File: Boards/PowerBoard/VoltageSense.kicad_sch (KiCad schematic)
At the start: 40 parts

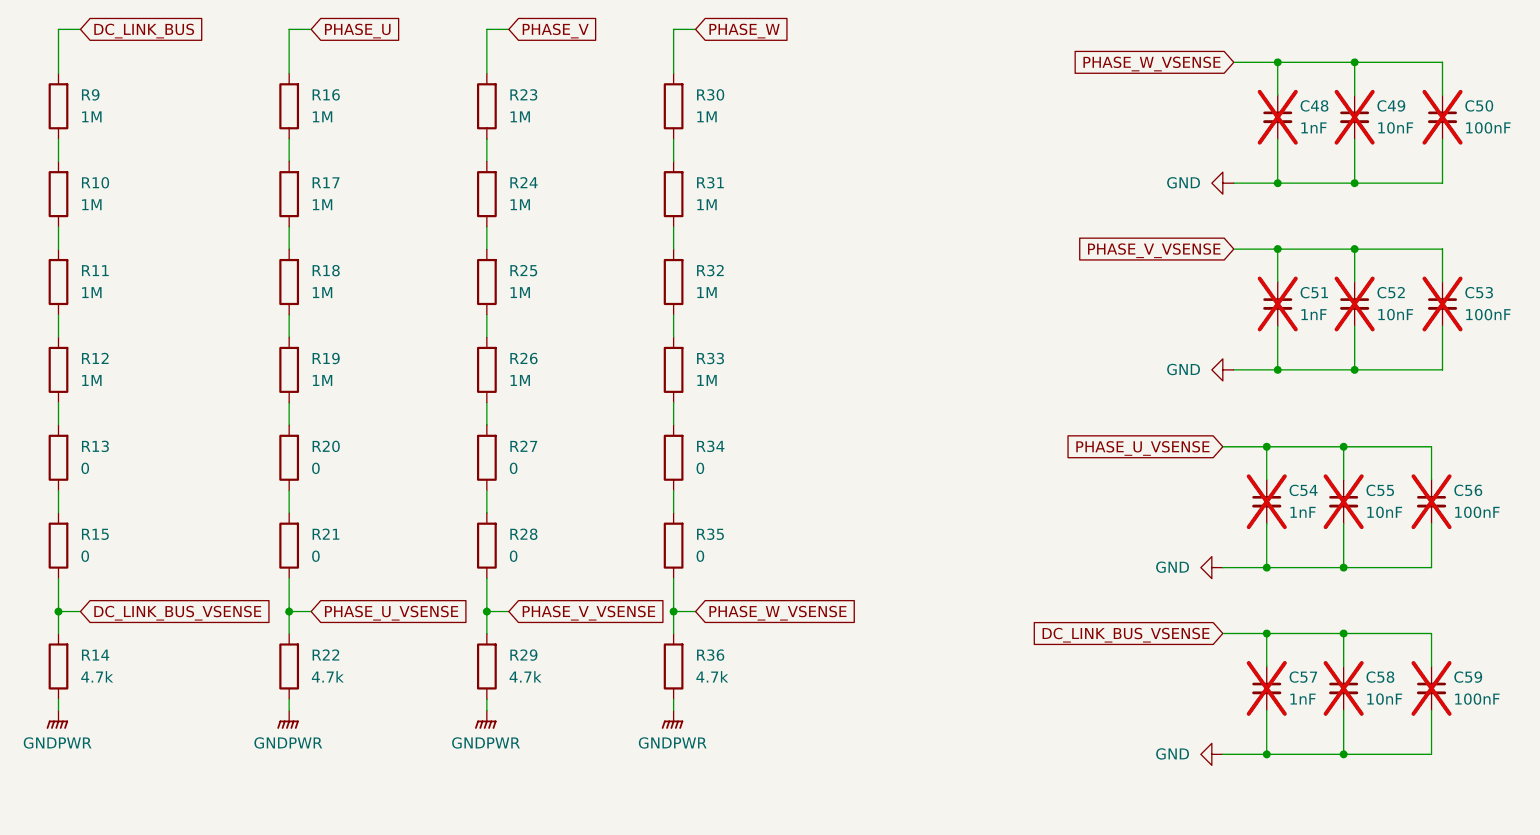
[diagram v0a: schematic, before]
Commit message: Add Zeners to Power Board
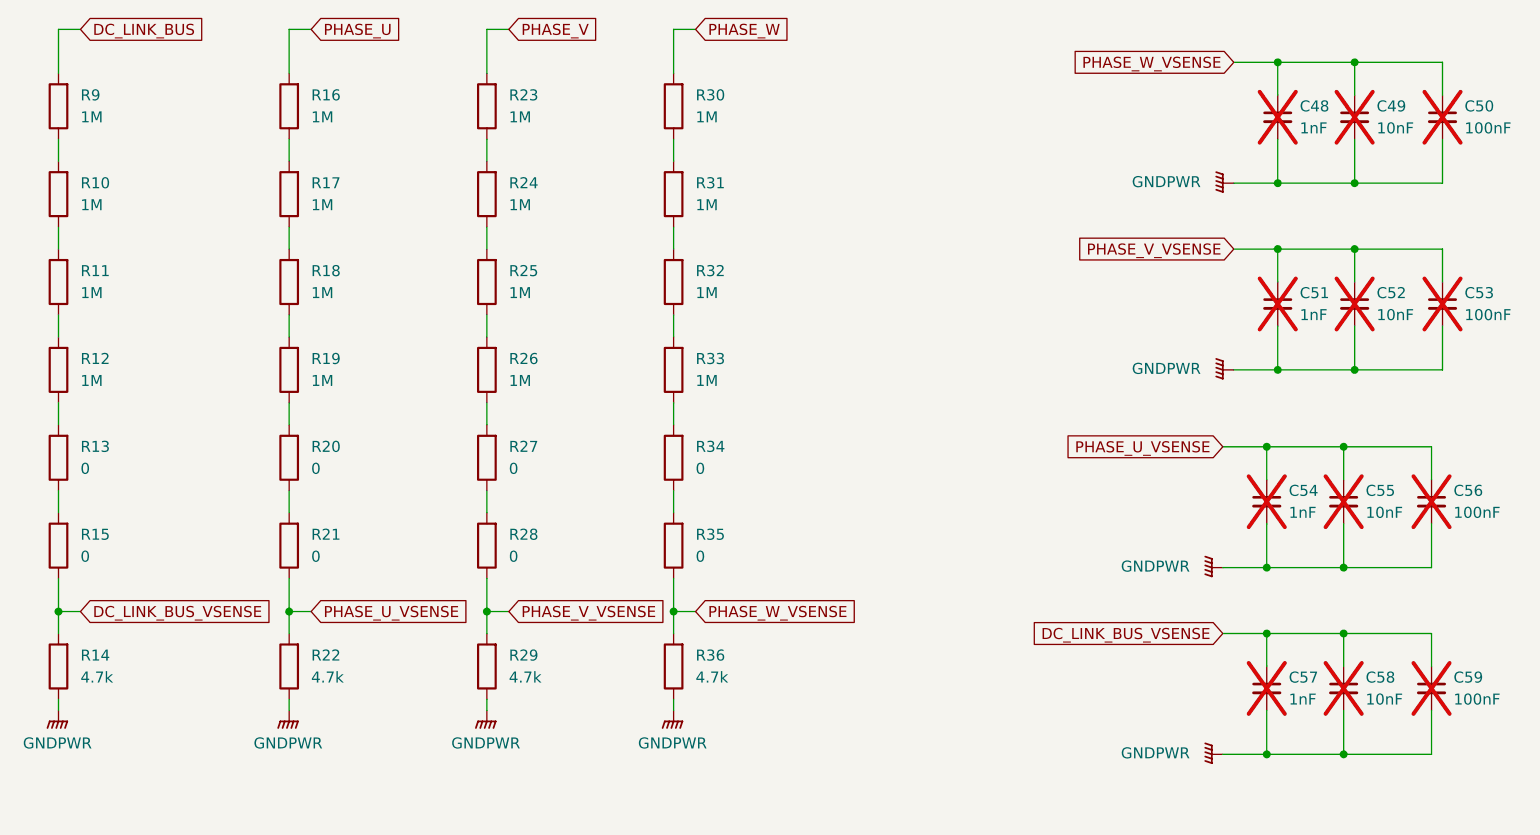
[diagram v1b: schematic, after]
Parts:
- C49, C50, C52, C53, C55, C56, C58, C59: footprint Capacitor_SMD:C_1210_3225Metric_Pad1.33x2.70mm_HandSolde -> Capacitor_SMD:C_1210_3225Metric_Pad1.33x2.70mm_HandSolder
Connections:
- net GND is gone; now on net GNDPWR: C48.2, C49.2, C50.2, C51.2, C52.2, C53.2, C54.2, C55.2, C56.2, C57.2, C58.2, C59.2

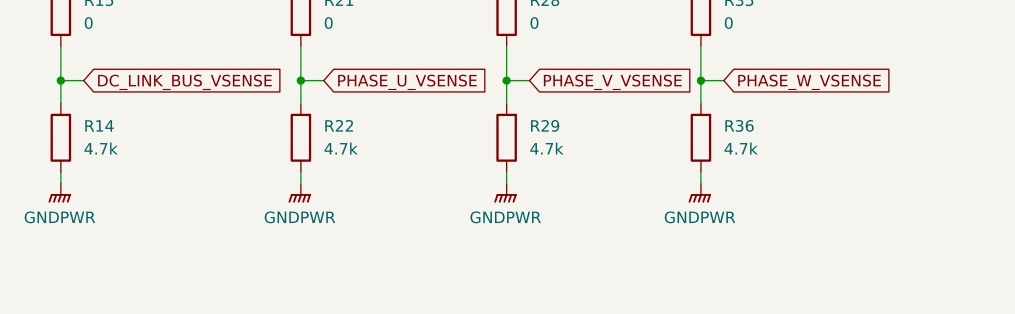
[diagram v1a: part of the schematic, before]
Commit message: Update Dynamic Brake Board
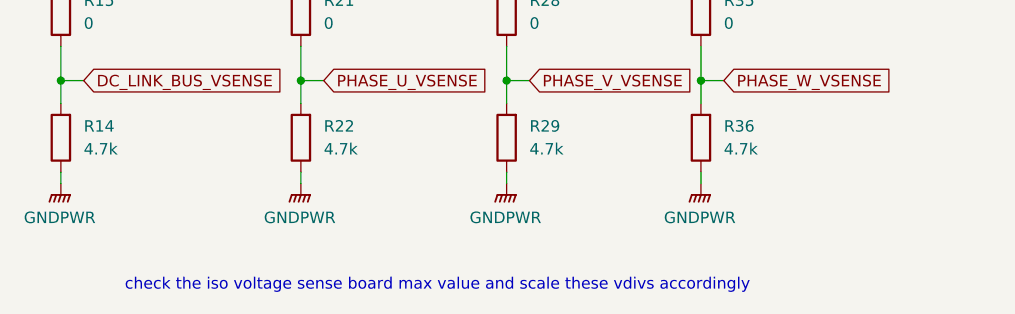
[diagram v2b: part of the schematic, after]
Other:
- note added: "check the iso voltage sense board max value and scale these vdivs accordingly"
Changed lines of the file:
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@@
 	(generator_version "9.0")
 	(paper "A4")
+	(text "check the iso voltage sense board max value and scale these vdivs accordingly"
+		(exclude_from_sim no)
+		(at 59.6268 106.5937 0)
+		(effects
+			(font
+				(size 1.27 1.27)
+			)
+		)
+	)
 	(junction
 		(at 158.75 55.88)

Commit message: Update Layouts
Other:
- note removed: "check the iso voltage sense board max value and scale these vdivs accordingly"
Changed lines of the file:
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@@
 	(generator_version "9.0")
 	(paper "A4")
-	(text "check the iso voltage sense board max value and scale these vdivs accordingly"
-		(exclude_from_sim no)
-		(at 59.6268 106.5937 0)
-		(effects
-			(font
-				(size 1.27 1.27)
-			)
-		)
-	)
 	(junction
 		(at 158.75 55.88)
